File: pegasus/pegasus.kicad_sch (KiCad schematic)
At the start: 21 parts, among them IC2 RFD900, IC3 L70B-M39, J1 Screw_Terminal_01x04, J2 Screw_Terminal_01x02, Q1 ST3413A, U1 Teensy4.0, U2 CON-SMA-EDGE-S, U3 CON-SMA-EDGE-S, U4 XTSD04GCLGEGA, U5 HT7350-A

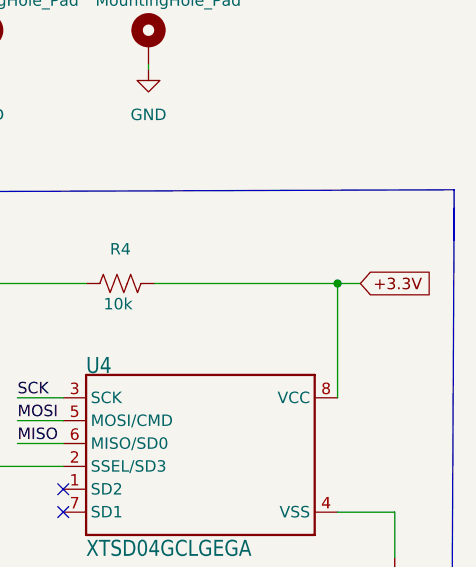
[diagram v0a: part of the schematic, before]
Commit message: route GND and 3.3V traces
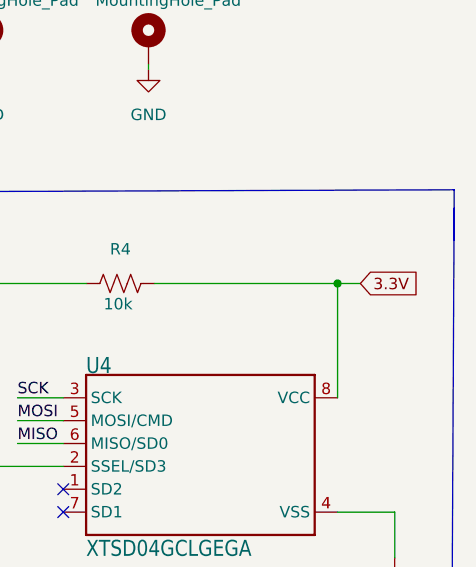
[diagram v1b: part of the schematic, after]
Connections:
- net +3.3V is gone; now on net 3.3V: R4.1, U4.8 (VCC)
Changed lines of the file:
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@@
+    (stroke (width 0) (type default) (color 0 0 0 0))
+  )
+  (wire (pts (xy 271.7038 49.7332) (xy 271.7038 62.4332))
     (stroke (width 0) (type default) (color 0 0 0 0))
   )
@@
   )
   (wire (pts (xy 85.09 43.18) (xy 95.25 43.18))
-    (stroke (width 0) (type default) (color 0 0 0 0))
-  )
-  (wire (pts (xy 271.7038 49.7332) (xy 271.7038 62.4332))
     (stroke (width 0) (type default) (color 0 0 0 0))
   )
@@
     (effects (font (size 1.27 1.27)) (justify left bottom))
   )
-  (global_label "+3.3V" (shape input) (at 274.2438 49.7332 0) (fields_autoplaced)
+  (global_label "3.3V" (shape input) (at 274.2438 49.7332 0) (fields_autoplaced)
     (effects (font (size 1.27 1.27)) (justify left))
-    (property "Intersheet References" "${INTERSHEET_REFS}" (id 0) (at 282.3417 49.8126 0)
+    (property "Intersheet References" "${INTERSHEET_REFS}" (id 0) (at 280.7693 49.6538 0)
       (effects (font (size 1.27 1.27)) (justify left) hide)
     )

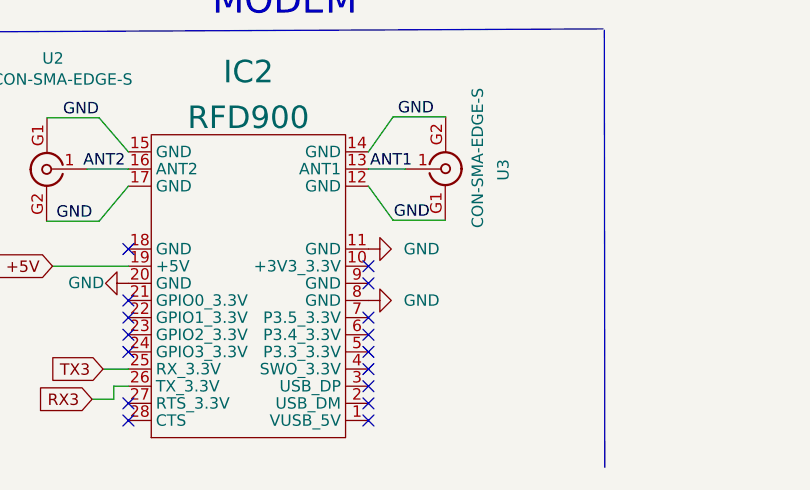
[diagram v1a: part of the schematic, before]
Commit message: add missing round pin to rfd900
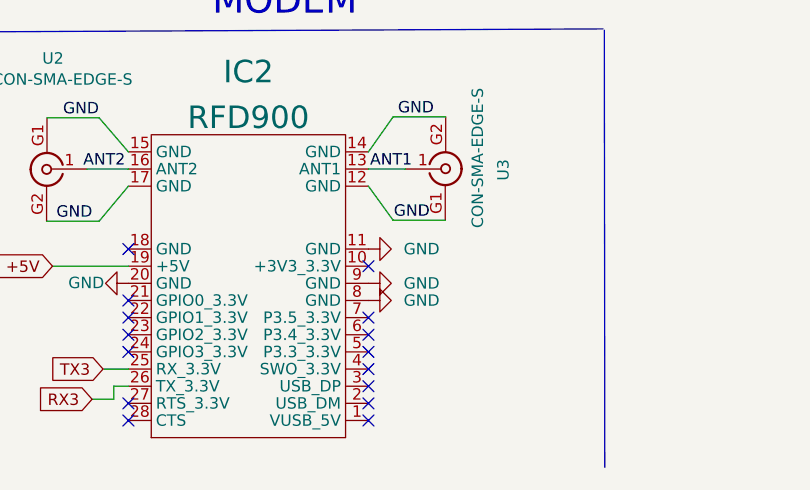
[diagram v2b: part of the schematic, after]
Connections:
- net GND: now also IC2.9 (GND)
- no-connect marks 60 -> 59
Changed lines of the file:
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@@
   (no_connect (at 119.2784 182.88))
   (no_connect (at 97.3836 109.22))
-  (no_connect (at 145.9484 177.165))
   (no_connect (at 145.9484 188.595))
   (no_connect (at 119.2784 180.975))
@@
     (pin "1")
   )
+  (symbol (lib_id "power:GND") (at 145.9484 177.165 90) (unit 1)
+    (in_bom yes) (on_board yes) (fields_autoplaced)
+    (property "Reference" "#PWR?" (id 0) (at 152.2984 177.165 0)
+      (effects (font (size 1.27 1.27)) hide)
+    )
+    (property "Value" "GND" (id 1) (at 149.86 177.1649 90)
+      (effects (font (size 1.27 1.27)) (justify right))
+    )
+    (property "Footprint" "" (id 2) (at 145.9484 177.165 0)
+      (effects (font (size 1.27 1.27)) hide)
+    )
+    (property "Datasheet" "" (id 3) (at 145.9484 177.165 0)
+      (effects (font (size 1.27 1.27)) hide)
+    )
+    (pin "1")
+  )
   (symbol (lib_id "MPL3115A2_v0.2-eagle-import:CAP_CERAMIC0805-NOOUTLINE") (at 95.25 38.1 180) (unit 1)
     (in_bom yes) (on_board yes)
@@
       (reference "#PWR0104") (unit 1) (value "GND") (footprint "")
     )
+    (path "/5d78c148-9a14-4651-8745-1c2c59b6d1dc"
+      (reference "#PWR?") (unit 1) (value "GND") (footprint "")
+    )
     (path "/cd0dd716-3c84-4981-941e-545033f1c88f"

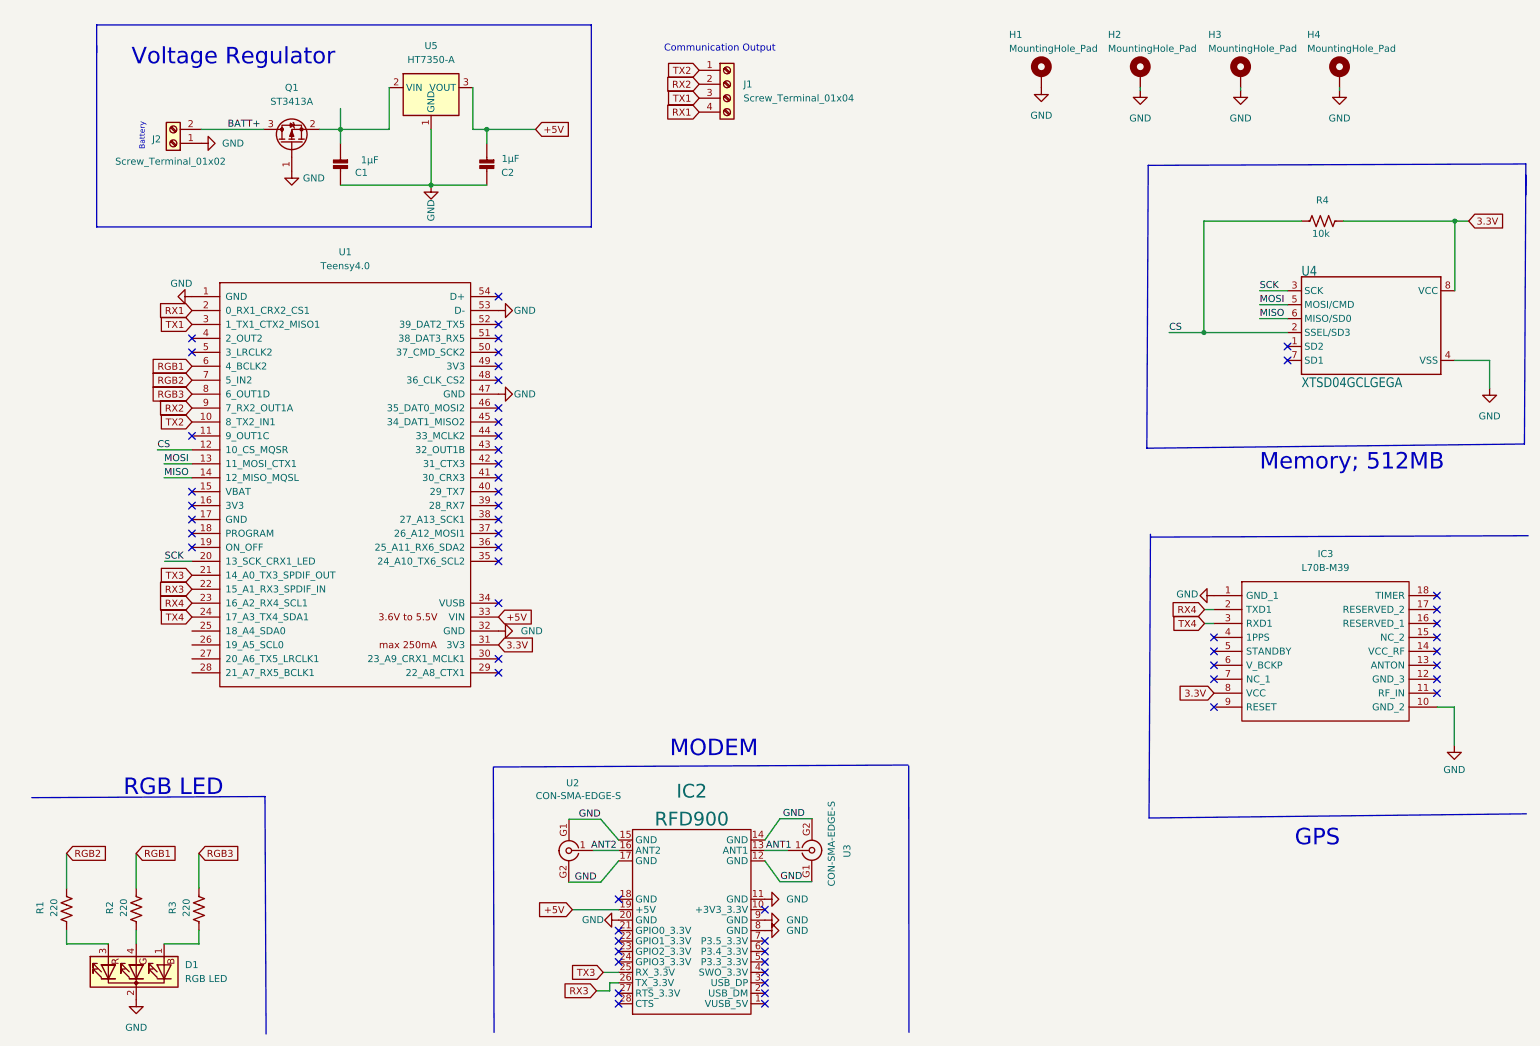
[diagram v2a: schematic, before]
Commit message: replace voltage regulator with 1A capable, variable regulator. Increase via size for PCB mill prototyping. Add more vias for RFD900
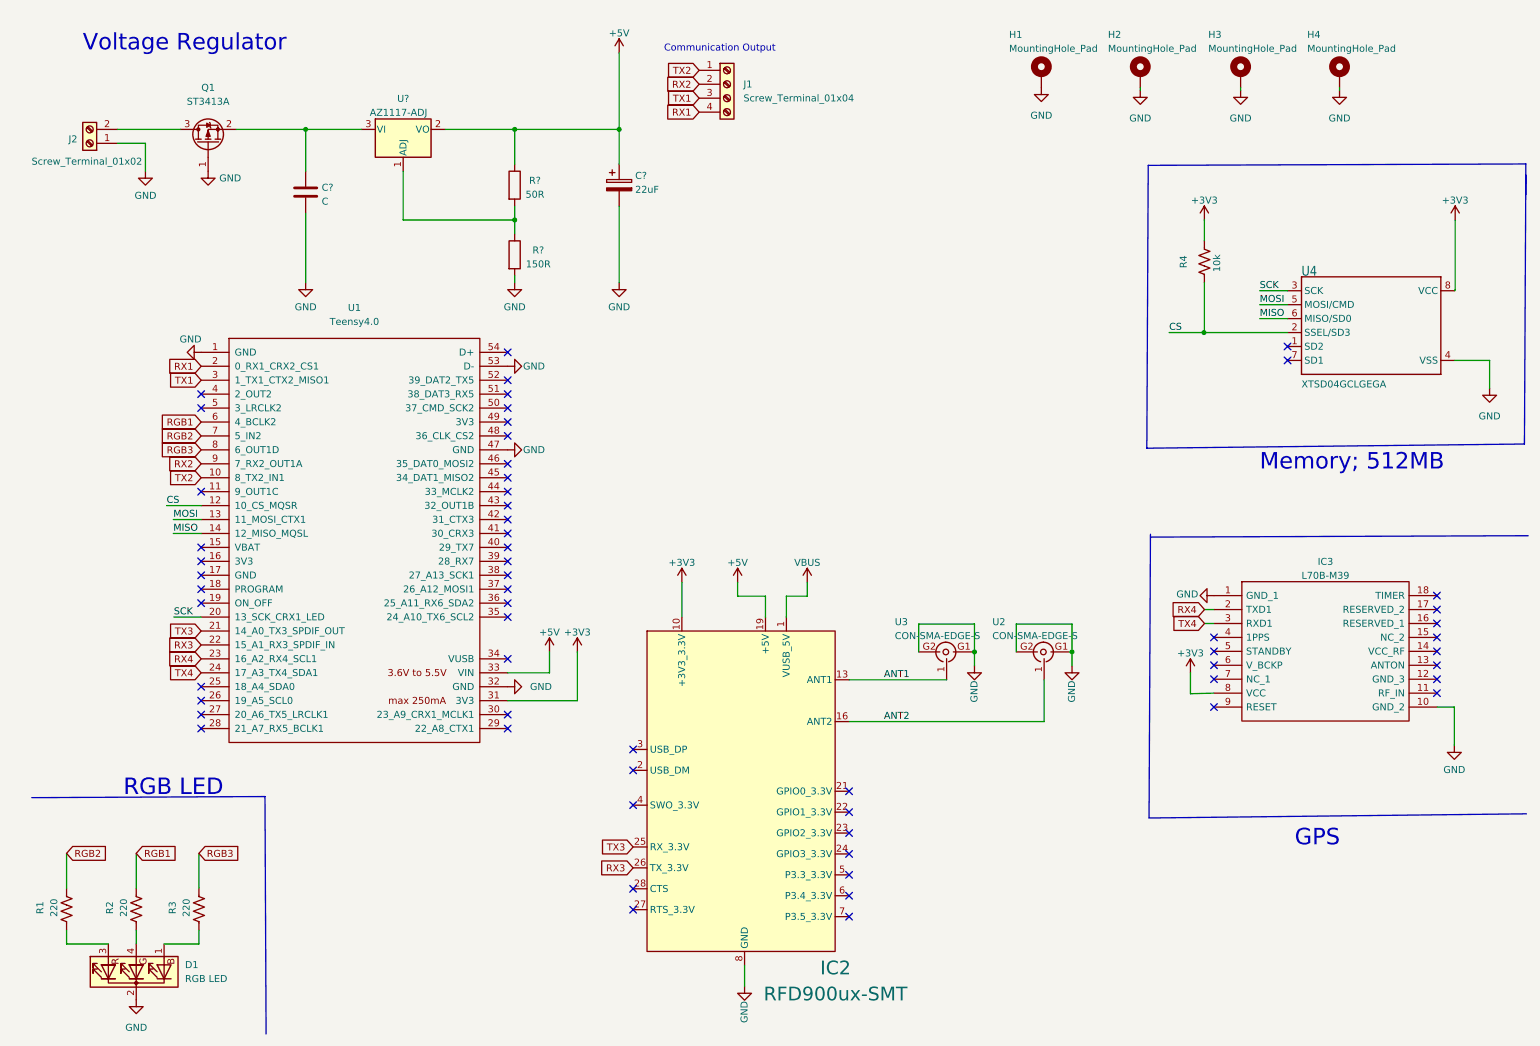
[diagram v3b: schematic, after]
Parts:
- removed C1, C2: 1µF, Capacitor_SMD:C_0805_2012Metric_Pad1.18x1.45mm_HandSolder, symbol MPL3115A2_v0.2-eagle-import:CAP_CERAMIC0805-NOOUTLINE
- removed U5: HT7350-A, Package_TO_SOT_SMD:SOT-89-3, symbol Regulator_Linear:HT75xx-1-SOT89
- added C?: C, Capacitor_SMD:C_0805_2012Metric, symbol Device:C
- added C?: 22uF, Capacitor_Tantalum_SMD:CP_EIA-7343-30_AVX-N, symbol Device:C_Polarized
- added R?: 50R, Capacitor_SMD:C_0402_1005Metric, symbol Device:R
- added R?: 150R, Capacitor_SMD:C_0402_1005Metric, symbol Device:R
- added U?: AZ1117-ADJ, Package_TO_SOT_SMD:SOT-223-3_TabPin2, symbol Regulator_Linear:AZ1117-ADJ
- H3, H4: footprint MountingHole:MountingHole_3.2mm_M3_Pad_Via -> MountingHole:MountingHole_3.2mm_M3_Pad
- IC2: value RFD900 -> RFD900ux-SMT
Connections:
- net 3.3V is gone; now on net +3V3: IC3.8 (VCC), R4.1, U1.31 (3V3), U4.8 (VCC)
- net +5V: now also C?.1, R?.1, U?.2 (VO)
- net GND: now also IC2.18 (GND), C?.2, C?.2, R?.2
- net at Q1.2 (S): now also C?.1, U?.3 (VI)
- net VBUS: now reaches IC2.1 (VUSB_5V)
- net +3V3: now reaches IC2.10 (+3V3_3.3V)
- net BATT+: no longer names the net of J2.2 (Pin_2), Q1.3 (D)
- new net: R?.1, R?.2, U?.1 (ADJ)
- no-connect marks 59 -> 60
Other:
- note removed: "Battery"
- note removed: "MODEM"
- moved on the sheet: J2, Q1, R4, U1, U2, U3

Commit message: add headings to and general clean up to schematic
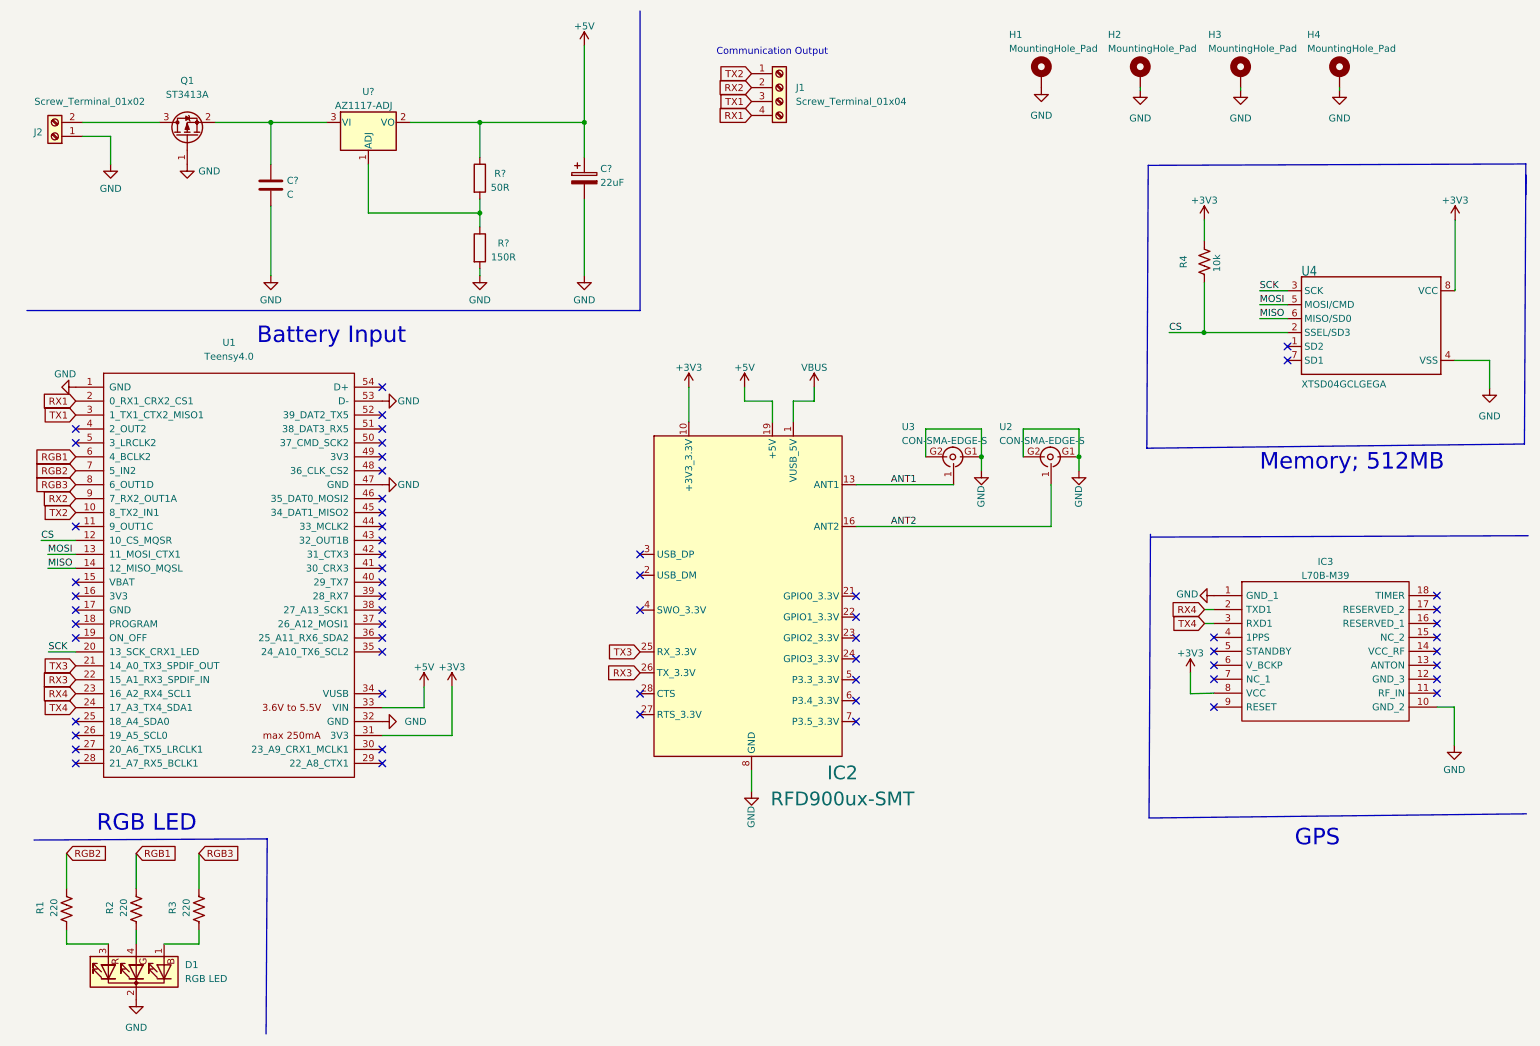
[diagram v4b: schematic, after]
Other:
- note added: "Battery Input"
- note removed: "Voltage Regulator"
- moved on the sheet: C?, IC2, J1, J2, Q1, R?, U1, U2, U3, U?

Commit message: reposition GPS to center of board, add gps reset circuitry
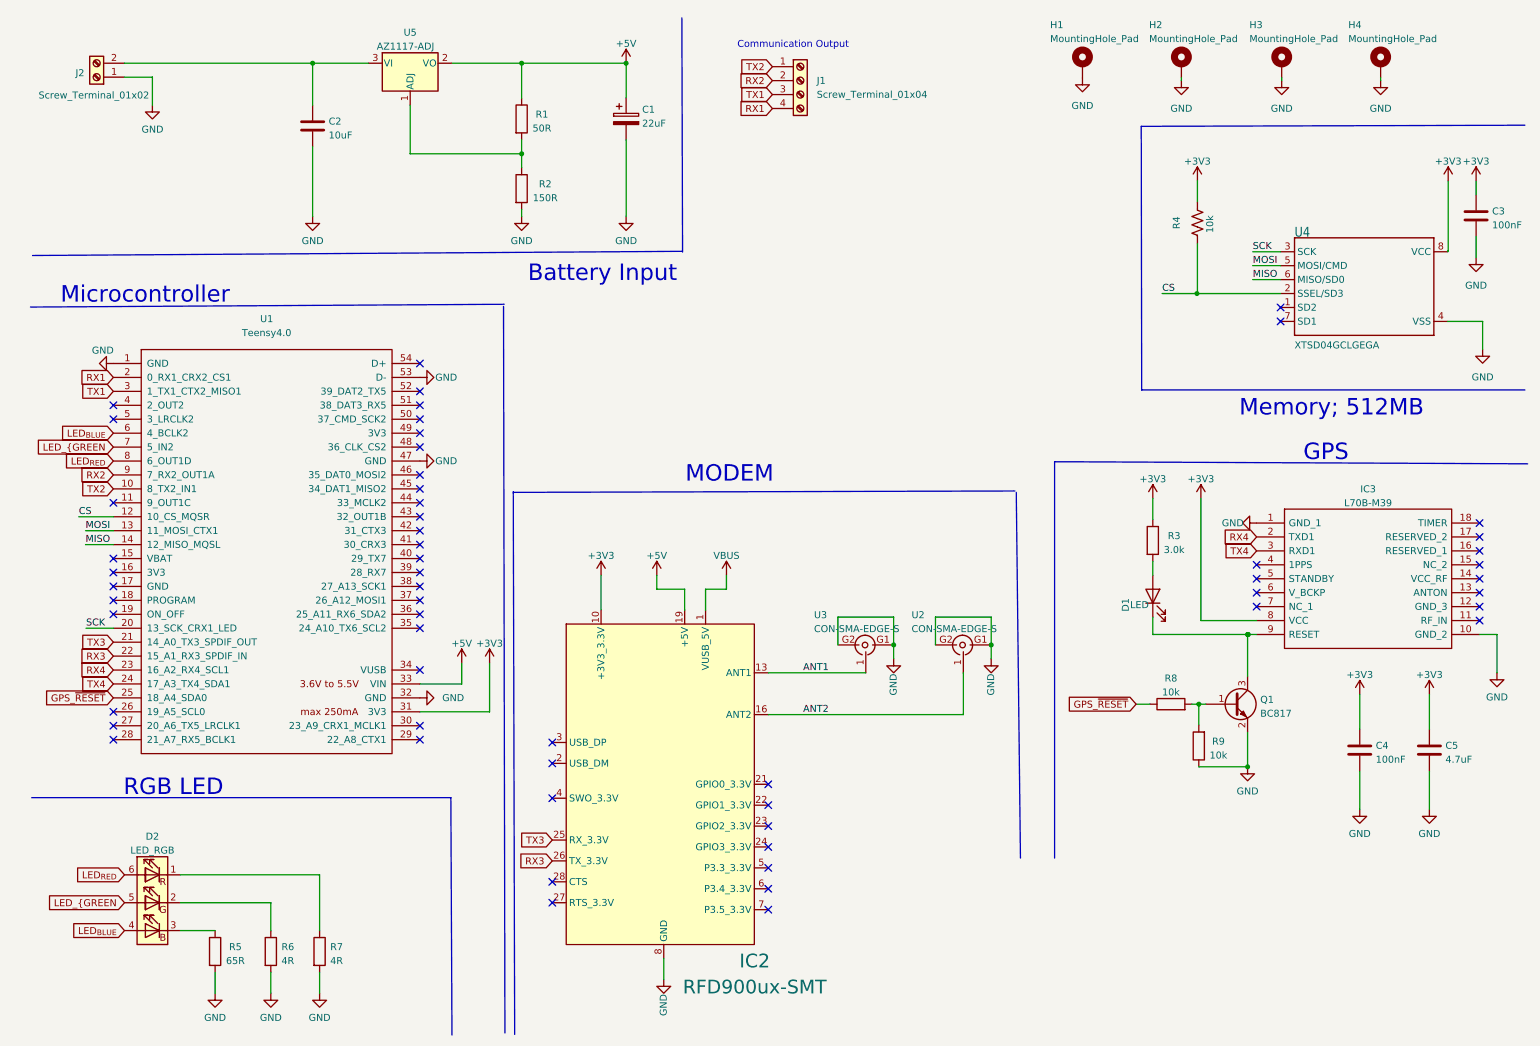
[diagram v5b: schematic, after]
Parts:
- removed D1: RGB LED, LED_THT:LED_D5.0mm-4_RGB, symbol Device:LED_BKRG
- removed Q1: ST3413A, Package_TO_SOT_SMD:SOT-23, symbol Transistor_FET:TSM2301ACX
- removed R1, R2, R3: 220, Resistor_SMD:R_1206_3216Metric_Pad1.30x1.75mm_HandSolder, symbol Device:R_US
- added C3, C4: 100nF, Capacitor_SMD:C_0805_2012Metric, symbol Device:C
- added C5: 4.7uF, Capacitor_SMD:C_1206_3216Metric, symbol Device:C
- added D1: LED, LED_SMD:LED_miniPLCC_2315, symbol Device:LED
- added D2: LED_RGB, LED_SMD:LED_RGB_5050-6, symbol Device:LED_RGB
- added Q1: BC817, Package_TO_SOT_SMD:SOT-23, symbol Transistor_BJT:BC817
- added R3: 3.0k, Resistor_SMD:R_0603_1608Metric, symbol Device:R
- added R5: 65R, Resistor_SMD:R_0603_1608Metric, symbol Device:R
- added R6, R7: 4R, Resistor_SMD:R_0603_1608Metric, symbol Device:R
- added R8, R9: 10k, Resistor_SMD:R_0603_1608Metric, symbol Device:R
- C2: renamed from C?; value C -> 10uF
- R4: footprint Resistor_SMD:R_0805_2012Metric_Pad1.20x1.40mm_HandSolder -> Resistor_SMD:R_0603_1608Metric
- gave numbers to parts that had none: 4
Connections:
- net +3V3: now also C3.1, C4.1, C5.1, R3.1
- net GND: now also C3.2, C4.2, C5.2, Q1.2 (E), R5.2, R6.2, R7.2, R9.1
- net GPS_~{RESET}: now reaches U1.25 (18_A4_SDA0)
- net GPS_~{RESET}: now also R8.1
- net at J2.2 (Pin_2): now also C2.1, U5.3 (VI)
- net at IC3.9 (RESET): now also D1.1 (K), Q1.3 (C)
- net RGB1 renamed LED_{BLUE}
- net LED_{BLUE}: now also D2.4 (BA)
- net RGB2 renamed LED_{GREEN
- net LED_{GREEN: now also D2.5 (GA)
- net RGB3 renamed LED_{RED}
- net LED_{RED}: now also D2.6 (RA)
- new net: Q1.1 (B), R8.2, R9.2
- new net: D1.2 (A), R3.2
- new net: D2.2 (GK), R6.1
- new net: D2.1 (RK), R7.1
- new net: D2.3 (BK), R5.1
- no-connect marks 60 -> 58
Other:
- note added: "MODEM"
- note added: "Microcontroller"
- moved on the sheet: C1, C2, H1, H2, H3, H4, IC2, IC3, J1, J2, R1, R2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
